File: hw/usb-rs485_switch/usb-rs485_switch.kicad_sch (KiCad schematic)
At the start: 136 parts, among them J1 RJ45_LED_Shielded, J10 VCC_OUT2, J11 5V_OUT1, J12 5V_OUT2, J13 3V_OUT1, J14 3V3_OUT2, J15 MC-107DM, J16 ISO_SHORT, J17 USB_NONISO, J18 RJ45_LED_Shielded, J19 RJ45_LED_Shielded, J2 RJ45_LED_Shielded, J20 RJ45_LED_Shielded, J21 RJ45_LED_Shielded, J22 RJ45_LED_Shielded, J23 RJ45_LED_Shielded, J24 Conn_02x08_Odd_Even, J25 USB_ISO, J26 Conn_01x03_Male, J27 USART3, J3 USART2, J4 I2C, J5 SPI, J6 GPIO, J7 PROG, J8 POWER, J9 VCC_OUT1, U1 74HC595, U10 XL1509-5.0E1, U11 AMS1117-3.3, U2 CD4051B, U28 SRV05-4, U29 SRV05-4, U3 74HC595, U4 74HC595, U5 74HC595, U6 STM32F103C8Tx, U7 ADUM4160, U8 M24C01-WMN, U9 TPS5430DDA, Y1 Crystal_GND23

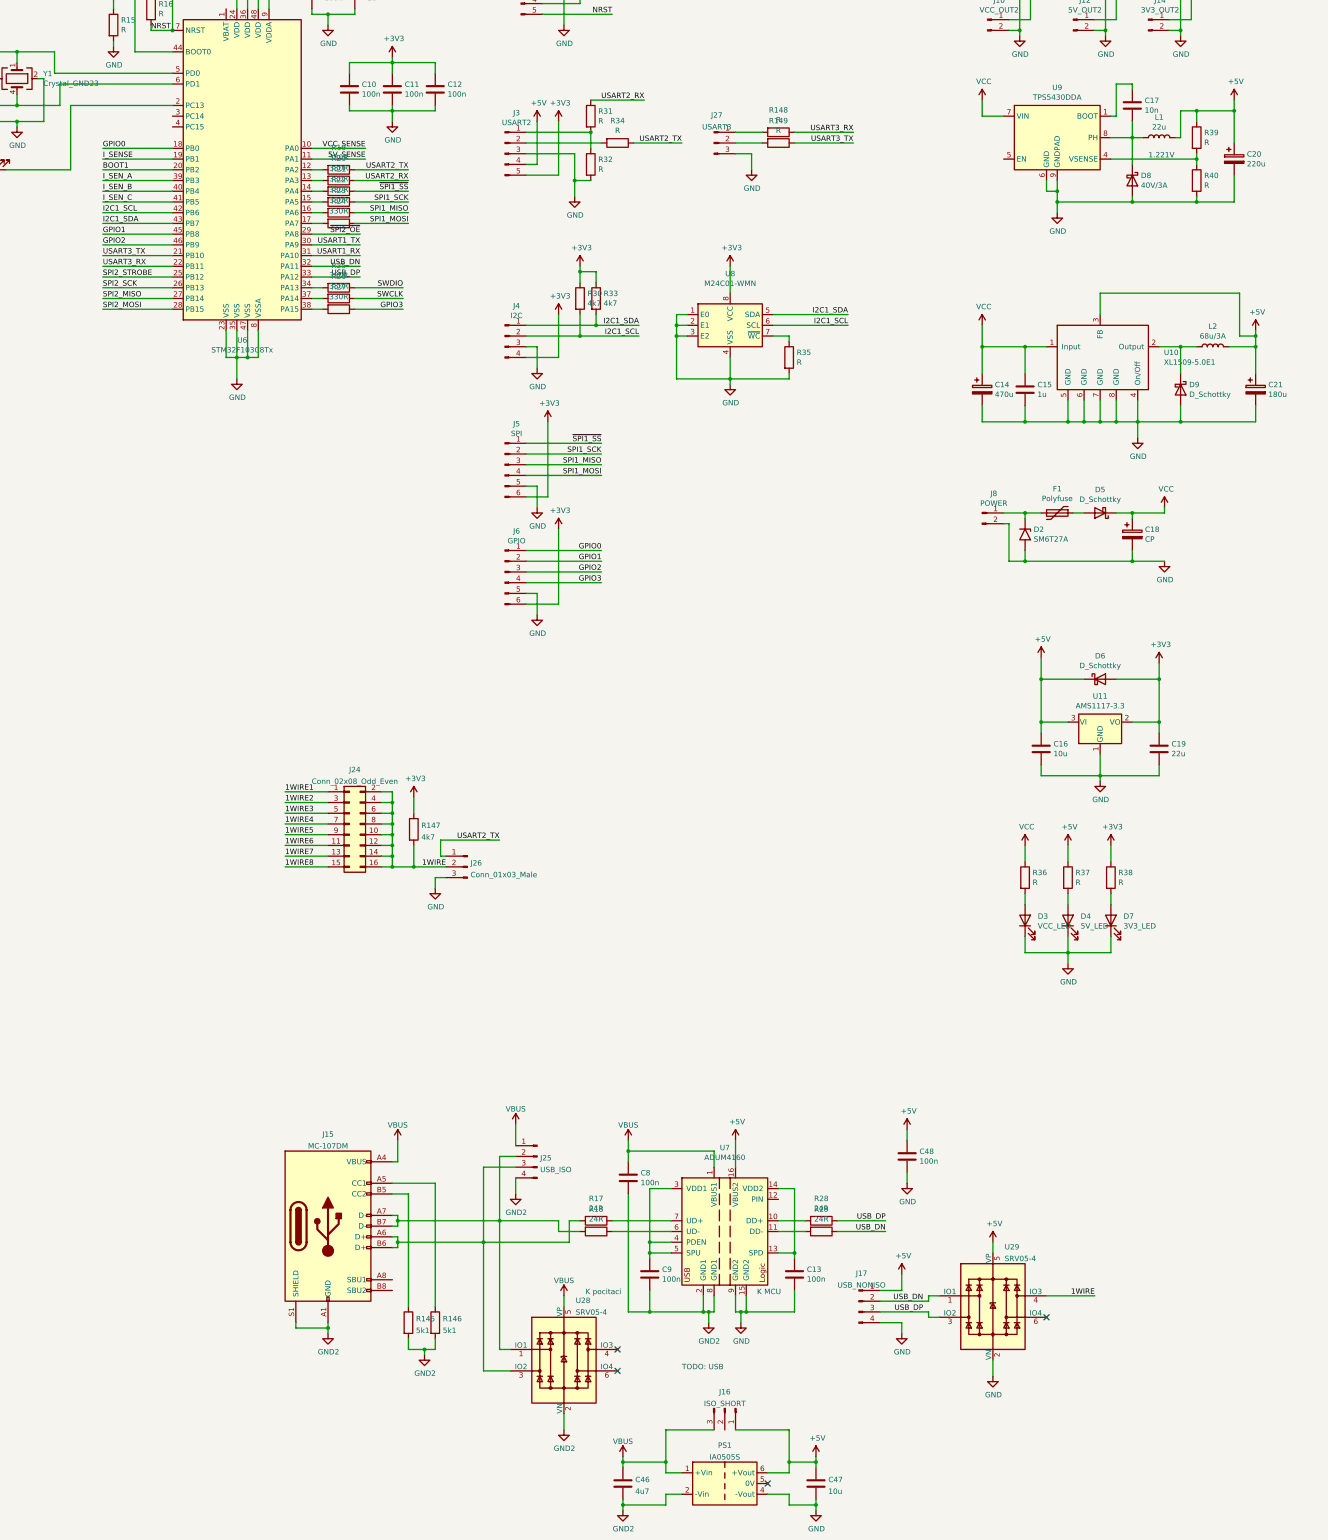
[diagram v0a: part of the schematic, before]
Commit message: Added 1wire and power selection jumpers.
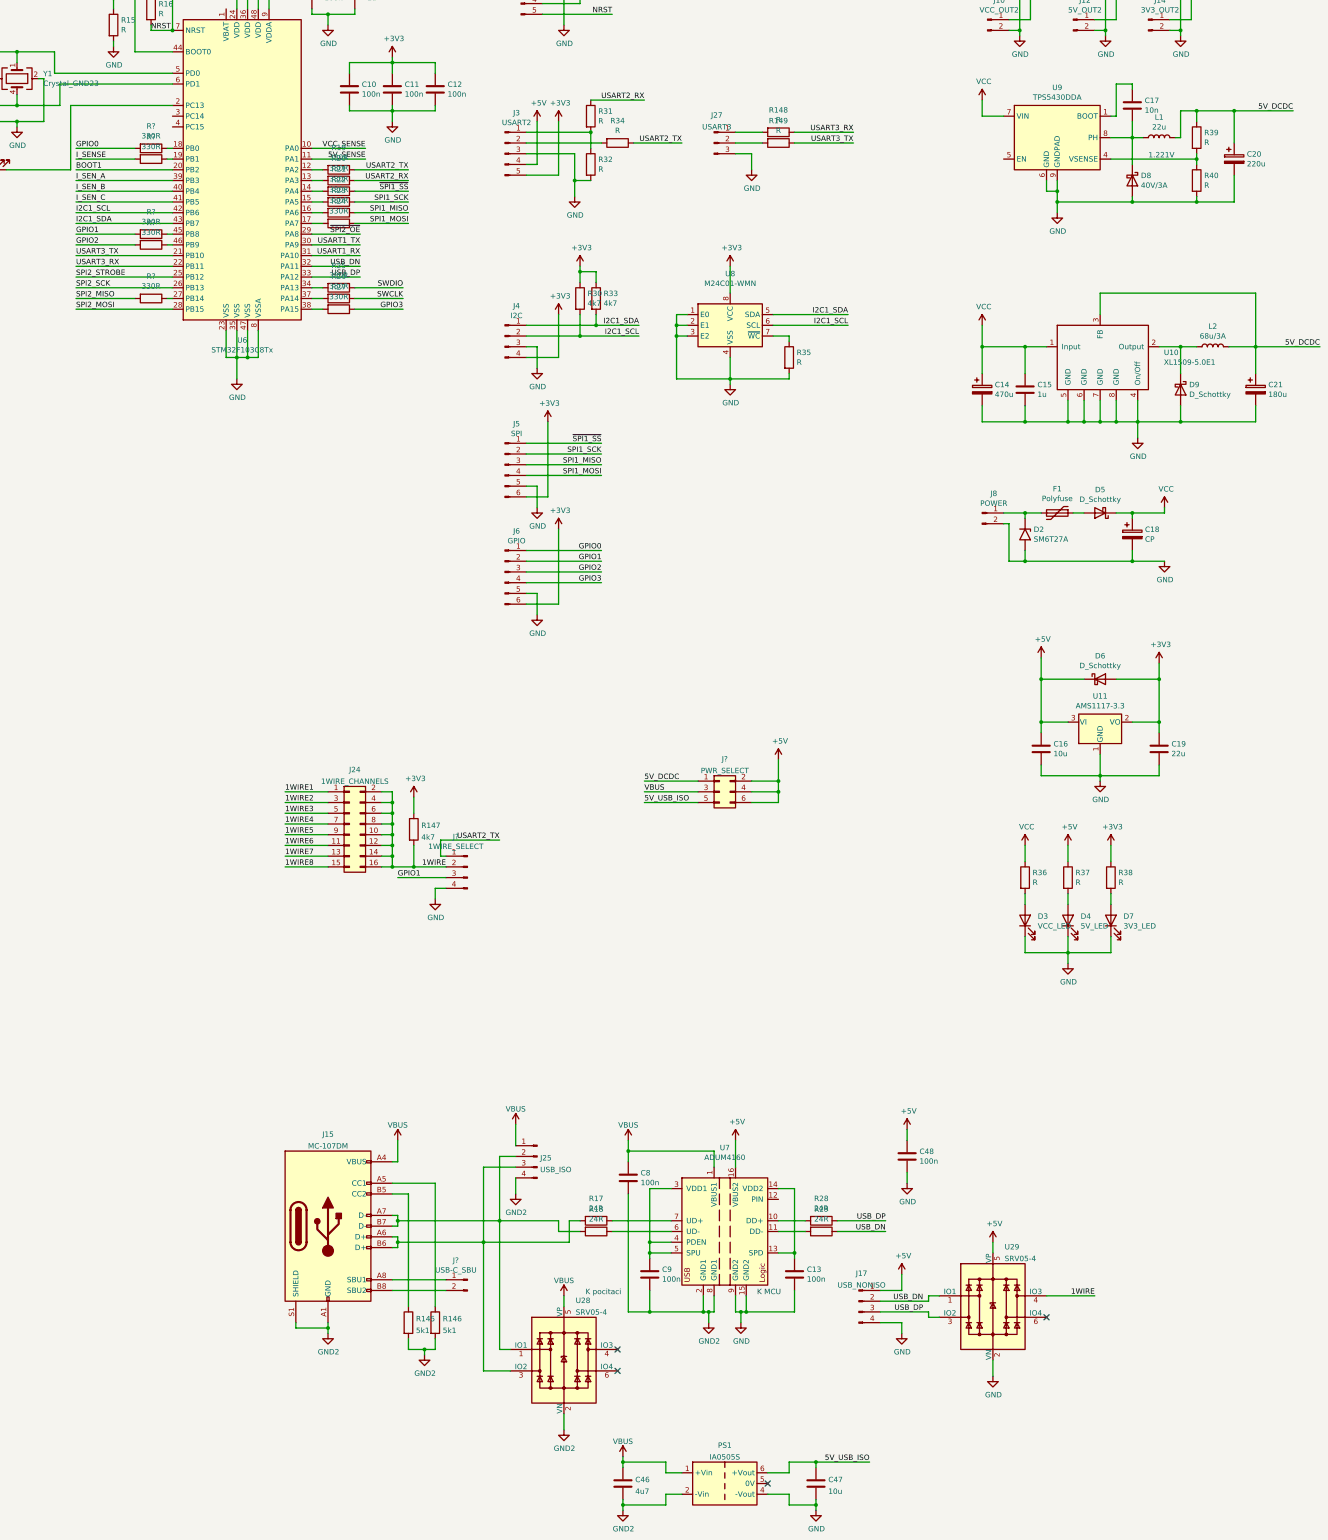
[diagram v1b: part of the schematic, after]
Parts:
- removed J16: ISO_SHORT, symbol Connector:Conn_01x03_Male
- removed J26: Conn_01x03_Male, symbol Connector:Conn_01x03_Male
- added J?: PWR_SELECT, symbol Connector_Generic:Conn_02x03_Odd_Even
- added J?: 1WIRE_SELECT, symbol Connector:Conn_01x04_Male
- added J?: USB-C_SBU, symbol Connector:Conn_01x02_Male
- added R? (x5): 330R, symbol Device:R
- J24: value Conn_02x08_Odd_Even -> 1WIRE_CHANNELS
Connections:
- net +5V: now also J?.2 (Pin_2), J?.4 (Pin_4), J?.6 (Pin_6); no longer C20.1, C21.1, C47.1, L1.2, L2.2, PS1.6 (+Vout), R39.1, U10.3 (FB)
- net 1WIRE: now also J?.2 (Pin_2)
- net GND: now also J?.4 (Pin_4)
- net GPIO0: now also R?.2; no longer U6.18 (PB0)
- net GPIO1: now also J?.3 (Pin_3), R?.2; no longer U6.45 (PB8)
- net GPIO2: now also R?.2; no longer U6.46 (PB9)
- net I_SENSE: now also R?.2; no longer U6.19 (PB1)
- net SPI2_MISO: now also R?.2; no longer U6.27 (PB14)
- net USART2_TX: now also J?.1 (Pin_1)
- net VBUS: now also J?.3 (Pin_3)
- net at J15.A8 (SBU1): now also J?.1 (Pin_1)
- net at J15.B8 (SBU2): now also J?.2 (Pin_2)
- new net: R?.1, U6.18 (PB0)
- new net: R?.1, U6.19 (PB1)
- new net: R?.1, U6.27 (PB14)
- new net: R?.1, U6.45 (PB8)
- new net: R?.1, U6.46 (PB9)
- new net 5V_DCDC: C20.1, C21.1, J?.1 (Pin_1), L1.2, L2.2, R39.1, U10.3 (FB)
- new net 5V_USB_ISO: C47.1, J?.5 (Pin_5), PS1.6 (+Vout)
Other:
- note removed: "TODO: USB"

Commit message: Assigned footprints, started routing.
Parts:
- added J16: RES1, Connector_PinHeader_2.54mm:PinHeader_1x03_P2.54mm_Vertical, symbol Connector:Conn_01x03_Male
- added J26: RES2, Connector_PinHeader_2.54mm:PinHeader_1x03_P2.54mm_Vertical, symbol Connector:Conn_01x03_Male
- added J28: RES3, Connector_PinHeader_2.54mm:PinHeader_1x03_P2.54mm_Vertical, symbol Connector:Conn_01x03_Male
- added J29: RES4, Connector_PinHeader_2.54mm:PinHeader_1x03_P2.54mm_Vertical, symbol Connector:Conn_01x03_Male
- added J30: RES5, Connector_PinHeader_2.54mm:PinHeader_1x03_P2.54mm_Vertical, symbol Connector:Conn_01x03_Male
- added J31: RES6, Connector_PinHeader_2.54mm:PinHeader_1x03_P2.54mm_Vertical, symbol Connector:Conn_01x03_Male
- added J32: RES7, Connector_PinHeader_2.54mm:PinHeader_1x03_P2.54mm_Vertical, symbol Connector:Conn_01x03_Male
- added J33: RES8, Connector_PinHeader_2.54mm:PinHeader_1x03_P2.54mm_Vertical, symbol Connector:Conn_01x03_Male
- C10, C11, C12, C13, C16, C17, C19, C4, C46, C47, C48, C49, C5, C50, C6, C7, C8, C9: footprint (none) -> Capacitor_SMD:C_0603_1608Metric
- D1: footprint (none) -> LED_SMD:LED_0603_1608Metric; LCSC (none) -> C72038
- D3, D4, D7: footprint (none) -> LED_SMD:LED_0603_1608Metric; LCSC (none) -> C72043
- D5, D6: value D_Schottky -> SS54; footprint (none) -> Diode_SMD:D_SMA; LCSC (none) -> C22452
- D8: value 40V/3A -> SS54; footprint (none) -> Diode_SMD:D_SMA; LCSC (none) -> C22452
- D9: value D_Schottky -> SS54; footprint (none) -> Diode_SMD:D_SMA
- F1: footprint (none) -> Fuse:Fuse_2920_7451Metric
- J1, J18, J19, J2, J20, J21, J22, J23: footprint (none) -> Connector_RJ:RJ45_Amphenol_RJHSE538X
- J10, J11, J12, J13, J14, J9: footprint (none) -> Connector_PinHeader_2.54mm:PinHeader_1x02_P2.54mm_Vertical
- J17, J25, J4: footprint (none) -> Connector_PinHeader_2.54mm:PinHeader_1x04_P2.54mm_Vertical
- J24: footprint (none) -> Connector_PinHeader_2.54mm:PinHeader_2x08_P2.54mm_Vertical
- J27: footprint (none) -> Connector_PinHeader_2.54mm:PinHeader_1x03_P2.54mm_Vertical
- J3: footprint (none) -> Connector_PinHeader_2.54mm:PinHeader_1x05_P2.54mm_Vertical
- J34: renamed from J?; footprint (none) -> Connector_PinHeader_2.54mm:PinHeader_1x04_P2.54mm_Vertical
- J35: renamed from J?; footprint (none) -> Connector_PinHeader_2.54mm:PinHeader_1x02_P2.54mm_Vertical
- J36: renamed from J?; footprint (none) -> Connector_PinHeader_2.54mm:PinHeader_2x03_P2.54mm_Vertical
- J5, J6: footprint (none) -> Connector_PinHeader_2.54mm:PinHeader_1x06_P2.54mm_Vertical
- J7: footprint (none) -> Connector_Molex:Molex_KK-254_AE-6410-05A_1x05_P2.54mm_Vertical
- J8: footprint (none) -> Connector_Phoenix_MC:PhoenixContact_MC_1,5_2-GF-3.81_1x02_P3.81mm_Horizontal_ThreadedFlange
- R1, R10, R11, R12, R13, R137, R138, R139, R14, R140, R141, R142, R143, R144, R145, R146, R147, R148, R149, R15, R16, R17, R18, R19, R2, R20, R21, R22, R23, R24, R25, R26, R27, R28, R29, R3, R30, R31, R32, R33, R34, R35, R36, R37, R38, R39, R4, R40, R5, R6, R7, R8, R9: footprint (none) -> Resistor_SMD:R_0603_1608Metric
- R150, R151, R152, R153, R154: renamed from R?; footprint (none) -> Resistor_SMD:R_0603_1608Metric
- TP1, TP2: footprint (none) -> TestPoint:TestPoint_THTPad_D2.0mm_Drill1.0mm
- U1, U3, U4, U5: footprint (none) -> Package_SO:SOIC-16_3.9x9.9mm_P1.27mm
- U2: footprint (none) -> Package_SO:SOIC-16_3.9x9.9mm_P1.27mm; LCSC (none) -> C2145
- U7: LCSC (none) -> C27586
- U8: LCSC (none) -> C79988
- Y1: footprint (none) -> Crystal:Crystal_SMD_3225-4Pin_3.2x2.5mm; LCSC (none) -> C13738
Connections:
- net at J1.1: now also J16.1 (Pin_1)
- net at J1.2: now also J16.2 (Pin_2)
- net at J1.3: now also J16.3 (Pin_3)
- net at J2.1: now also J26.1 (Pin_1)
- net at J2.2: now also J26.2 (Pin_2)
- net at J2.3: now also J26.3 (Pin_3)
- net at J18.1: now also J28.1 (Pin_1)
- net at J18.2: now also J28.2 (Pin_2)
- net at J18.3: now also J28.3 (Pin_3)
- net at J23.1: now also J33.1 (Pin_1)
- net at J23.2: now also J33.2 (Pin_2)
- net at J23.3: now also J33.3 (Pin_3)
- net at J22.1: now also J32.1 (Pin_1)
- net at J22.2: now also J32.2 (Pin_2)
- net at J22.3: now also J32.3 (Pin_3)
- net at J20.1: now also J30.1 (Pin_1)
- net at J20.2: now also J30.2 (Pin_2)
- net at J20.3: now also J30.3 (Pin_3)
- net at J19.1: now also J29.1 (Pin_1)
- net at J19.2: now also J29.2 (Pin_2)
- net at J19.3: now also J29.3 (Pin_3)
- net at J21.1: now also J31.1 (Pin_1)
- net at J21.2: now also J31.2 (Pin_2)
- net at J21.3: now also J31.3 (Pin_3)

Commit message: Routing in progress.
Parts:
- added H1, H2, H3, H4: MountingHole_Pad, MountingHole:MountingHole_3.2mm_M3_Pad_Via, symbol Mechanical:MountingHole_Pad
- C1, C2, C3: footprint (none) -> Capacitor_SMD:C_0603_1608Metric
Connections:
- net 1WIRE1: now also J24.15 (Pin_15); no longer J24.1 (Pin_1)
- net 1WIRE2: now also J24.13 (Pin_13); no longer J24.3 (Pin_3)
- net 1WIRE3: now also J24.11 (Pin_11); no longer J24.5 (Pin_5)
- net 1WIRE4: now also J24.9 (Pin_9); no longer J24.7 (Pin_7)
- net 1WIRE5: now also J24.7 (Pin_7); no longer J24.9 (Pin_9)
- net 1WIRE6: now also J24.5 (Pin_5); no longer J24.11 (Pin_11)
- net 1WIRE7: now also J24.3 (Pin_3); no longer J24.13 (Pin_13)
- net 1WIRE8: now also J24.1 (Pin_1); no longer J24.15 (Pin_15)
- net GND: now also H1.1, H2.1, H3.1, H4.1
- net LED_G2: now also R5.1; no longer R2.1
- net LED_G3: now also R2.1; no longer R3.1
- net LED_G4: now also R3.1; no longer R4.1
- net LED_G5: now also R6.1; no longer R5.1
- net LED_G6: now also R4.1; no longer R6.1
- net PWR_EN1: now also U1.5 (QF); no longer U3.15 (QA)
- net PWR_EN2: now also U1.1 (QB); no longer U3.1 (QB)
- net PWR_EN3: now also U3.5 (QF); no longer U3.2 (QC)
- net PWR_EN4: now also U3.1 (QB); no longer U3.3 (QD)
- net PWR_EN5: now also U4.5 (QF); no longer U3.4 (QE)
- net PWR_EN6: now also U4.1 (QB); no longer U3.5 (QF)
- net PWR_EN7: now also U5.5 (QF); no longer U3.6 (QG)
- net PWR_EN8: now also U5.1 (QB); no longer U3.7 (QH)
- net TX_EN1: now also U1.6 (QG); no longer U4.15 (QA)
- net TX_EN2: now also U1.2 (QC); no longer U4.1 (QB)
- net TX_EN3: now also U3.6 (QG); no longer U4.2 (QC)
- net TX_EN4: now also U3.2 (QC); no longer U4.3 (QD)
- net TX_EN5: now also U4.6 (QG); no longer U4.4 (QE)
- net TX_EN6: now also U4.2 (QC); no longer U4.5 (QF)
- net TX_EN7: now also U5.6 (QG); no longer U4.6 (QG)
- net TX_EN8: now also U5.2 (QC); no longer U4.7 (QH)
- net ~{RX_EN1}: now also U1.7 (QH); no longer U5.15 (QA)
- net ~{RX_EN2}: now also U1.3 (QD); no longer U5.1 (QB)
- net ~{RX_EN3}: now also U3.7 (QH); no longer U5.2 (QC)
- net ~{RX_EN4}: now also U3.3 (QD); no longer U5.3 (QD)
- net ~{RX_EN5}: now also U4.7 (QH); no longer U5.4 (QE)
- net ~{RX_EN6}: now also U4.3 (QD); no longer U5.5 (QF)
- net ~{RX_EN7}: now also U5.7 (QH); no longer U5.6 (QG)
- net ~{RX_EN8}: now also U5.3 (QD); no longer U5.7 (QH)
- net at R2.2: now also U3.4 (QE); no longer U1.1 (QB)
- net at U1.15 (QA): now also R5.2; no longer R1.2
- net at R3.2: now also U3.15 (QA); no longer U1.2 (QC)
- net at R4.2: now also U4.15 (QA); no longer U1.3 (QD)
- net at U1.4 (QE): now also R1.2; no longer R5.2
- net at R6.2: now also U4.4 (QE); no longer U1.5 (QF)
- net at R7.2: now also U5.4 (QE); no longer U1.6 (QG)
- net at R8.2: now also U5.15 (QA); no longer U1.7 (QH)
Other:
- moved on the sheet: C4, C5, R1, R2, R3, R4, R5, R6, R7, R8, U4, U5

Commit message: Routing in progress...
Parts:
- removed R154, R20: 330R, Resistor_SMD:R_0603_1608Metric, symbol Device:R
- removed TP2: NRST, TestPoint:TestPoint_THTPad_D2.0mm_Drill1.0mm, symbol Connector:TestPoint
- added C51, C52: 100n, Capacitor_SMD:C_0603_1608Metric, symbol Device:C
- added C53: 470u, symbol Device:CP
- added C54, C55, C56: 1u, symbol Device:C
- added C57: 180u, symbol Device:CP
- added C58, C63: 4u7/50V, Capacitor_SMD:C_1206_3216Metric, symbol Device:C
- added C59, C61: 8.2n, Capacitor_SMD:C_0603_1608Metric, symbol Device:C
- added C60: 22n, Capacitor_SMD:C_0603_1608Metric, symbol Device:C
- added C62: 22u/6.3V X5R, Capacitor_SMD:C_0603_1608Metric, symbol Device:C
- added D26: SS14, Diode_SMD:D_SMA, symbol Device:D_Schottky
- added L3: 47u, Inductor_SMD:L_Bourns_SRP7028A_7.3x6.6mm, symbol Device:L
- added L4: 68u/3A, symbol Device:L
- added R155, R156, R157, R158: R, Resistor_SMD:R_0603_1608Metric, symbol Device:R
- added U30: TPS54331, Package_SO:SOIC-8_3.9x4.9mm_P1.27mm, symbol user:TPS54331
- added U31: RY8310, Package_TO_SOT_SMD:SOT-23-6, symbol RY8310:RY8310
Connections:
- net +3V3: now also C51.1
- net +5V: no longer J3.4 (Pin_4)
- net 1WIRE: no longer U29.4 (IO3)
- net 5V_DCDC: now also R34.1, C56.1, C57.1, C62.1, L3.2, L4.2, R157.1
- net GND: now also C51.2, C53.2, C54.2, C57.2, C58.2, C59.2, C60.2, C61.2, C62.2, C63.2, D26.2 (A), R155.2, R158.2, U30.7 (GND), U30.9 (PAD), U31.2 (GND)
- net I_SENSE1: now also U2.1 (X4); no longer U2.13 (X0)
- net I_SENSE2: now also U2.5 (X5); no longer U2.14 (X1)
- net I_SENSE3: now also U2.2 (X6); no longer U2.15 (X2)
- net I_SENSE4: now also U2.4 (X7); no longer U2.12 (X3)
- net I_SENSE5: now also U2.15 (X2); no longer U2.1 (X4)
- net I_SENSE6: now also U2.14 (X1); no longer U2.5 (X5)
- net I_SENSE7: now also U2.13 (X0); no longer U2.2 (X6)
- net I_SENSE8: now also U2.12 (X3); no longer U2.4 (X7)
- net USART2_RX: now also U6.13 (PA3)
- net USART2_TX: now also J3.2 (Pin_2); no longer R34.1
- net VCC: now also C53.1, C54.1, C58.1, C63.1, U30.2 (VIN), U31.4 (EN), U31.5 (VIN)
- net USB_IN_P: now reaches J15.A6 (D+), J15.B6 (D+), J25.3 (Pin_3), R17.2, U28.3 (IO2)
- net USB_IN_N: now reaches J15.A7 (D-), J15.B7 (D-), J25.2 (Pin_2), R18.2, U28.1 (IO1)
- net at R34.2: now also C56.2, R155.1, U31.3 (FB); no longer J3.2 (Pin_2)
- new net: C55.1, U31.1 (BOOT)
- new net: C55.2, L4.1, U31.6 (SW)
- new net: C52.1, U30.1 (BOOT)
- new net: C61.1, U30.4 (SS)
- new net: R157.2, R158.1, U30.5 (VSENSE)
- new net: C59.1, R156.1, U30.6 (COMP)
- new net: C52.2, D26.1 (K), L3.1, U30.8 (PH)
- new net: C60.1, R156.2
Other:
- moved on the sheet: C14, C15, C17, C20, C21, D8, D9, L1, L2, R39, R40, U10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

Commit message: Routed.
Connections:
- net I_SENSE1: now also U2.4 (X7); no longer U2.1 (X4)
- net I_SENSE2: now also U2.2 (X6); no longer U2.5 (X5)
- net I_SENSE3: now also U2.1 (X4); no longer U2.2 (X6)
- net I_SENSE4: now also U2.5 (X5); no longer U2.4 (X7)
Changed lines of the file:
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@@
     (effects (font (size 1.27 1.27)) (justify left bottom))
   )
-  (label "I_SENSE4" (at 72.39 386.08 180)
+  (label "I_SENSE4" (at 72.39 381 180)
     (effects (font (size 1.27 1.27)) (justify right bottom))
   )
@@
     (effects (font (size 1.27 1.27)) (justify right bottom))
   )
-  (label "I_SENSE2" (at 72.39 381 180)
+  (label "I_SENSE2" (at 72.39 383.54 180)
     (effects (font (size 1.27 1.27)) (justify right bottom))
   )
@@
     (effects (font (size 1.27 1.27)) (justify right bottom))
   )
-  (label "I_SENSE1" (at 72.39 378.46 180)
+  (label "I_SENSE1" (at 72.39 386.08 180)
     (effects (font (size 1.27 1.27)) (justify right bottom))
   )
@@
     (effects (font (size 1.27 1.27)) (justify left bottom))
   )
-  (label "I_SENSE3" (at 72.39 383.54 180)
-    (effects (font (size 1.27 1.27)) (justify right bottom))
-  )
+  (label "I_SENSE3" (at 72.39 378.46 180)
+    (effects (font (size 1.27 1.27)) (justify right bottom))
+  )

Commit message: Removed unused DCDC, board labels.
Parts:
- removed C14, C53: 470u, symbol Device:CP
- removed C15, C54, C55, C56: 1u, symbol Device:C
- removed C17: 10n, Capacitor_SMD:C_0603_1608Metric, symbol Device:C
- removed C20: 220u, symbol Device:CP
- removed C21, C57: 180u, symbol Device:CP
- removed D8, D9: SS54, Diode_SMD:D_SMA, symbol Device:D_Schottky
- removed JP1: SolderJumper_2_Open, symbol Jumper:SolderJumper_2_Open
- removed L1: 22u, symbol Device:L
- removed L2, L4: 68u/3A, symbol Device:L
- removed R155, R34, R39, R40: R, Resistor_SMD:R_0603_1608Metric, symbol Device:R
- removed U10: XL1509-5.0E1, Package_SO:SO-8_5.3x6.2mm_P1.27mm, symbol xl1509:XL1509-5.0E1
- removed U31: RY8310, Package_TO_SOT_SMD:SOT-23-6, symbol RY8310:RY8310
- removed U9: TPS5430DDA, Package_SO:TI_SO-PowerPAD-8_ThermalVias, symbol Regulator_Switching:TPS5430DDA
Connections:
- net SBU1: now reaches J15.A8 (SBU1), J35.1 (Pin_1)
- net SBU2: now reaches J15.B8 (SBU2), J35.2 (Pin_2)
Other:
- note removed: "1.221V"
